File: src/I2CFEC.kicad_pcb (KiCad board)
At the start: 2 copper layers, 24 x 27.9 mm, 25 parts, among them J1 105444-0001, J2 B4B-XH-A, U1 PIC16F1454, U2 MIC2091

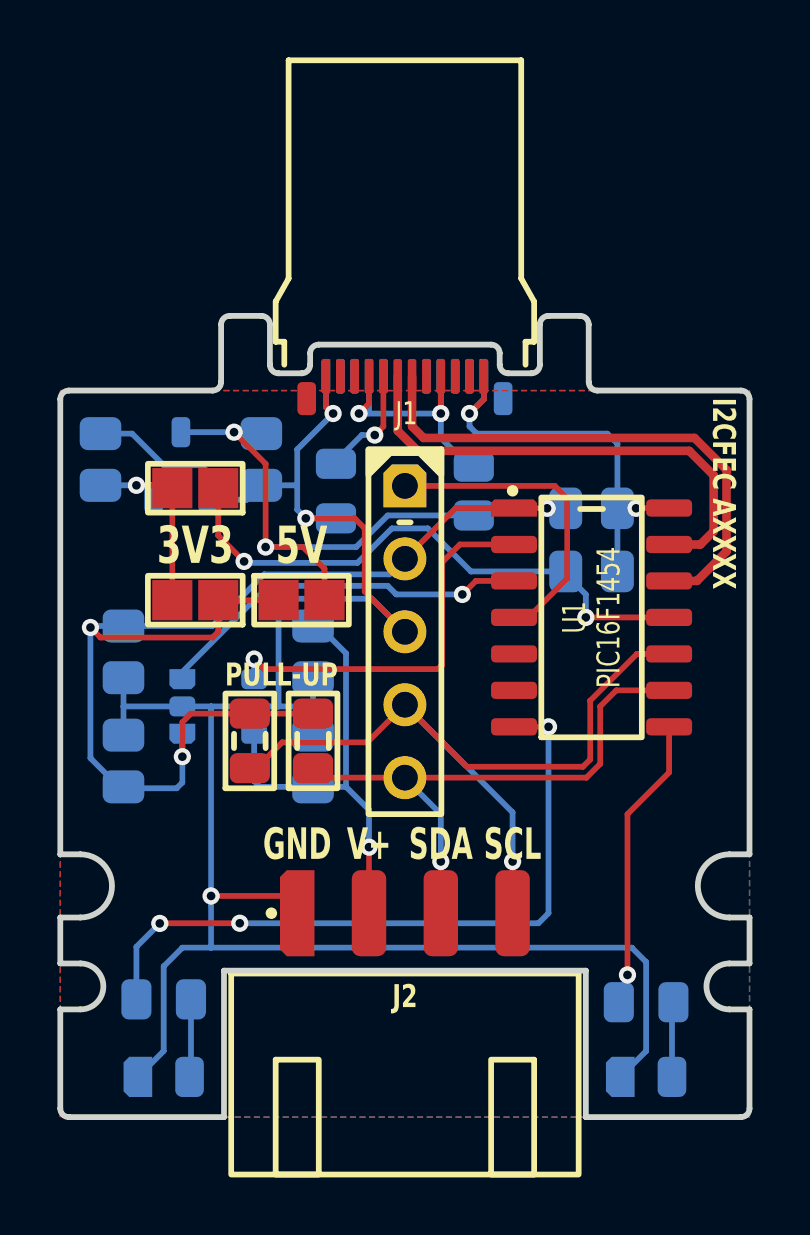
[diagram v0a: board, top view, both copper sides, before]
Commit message: Added pullup mosfet
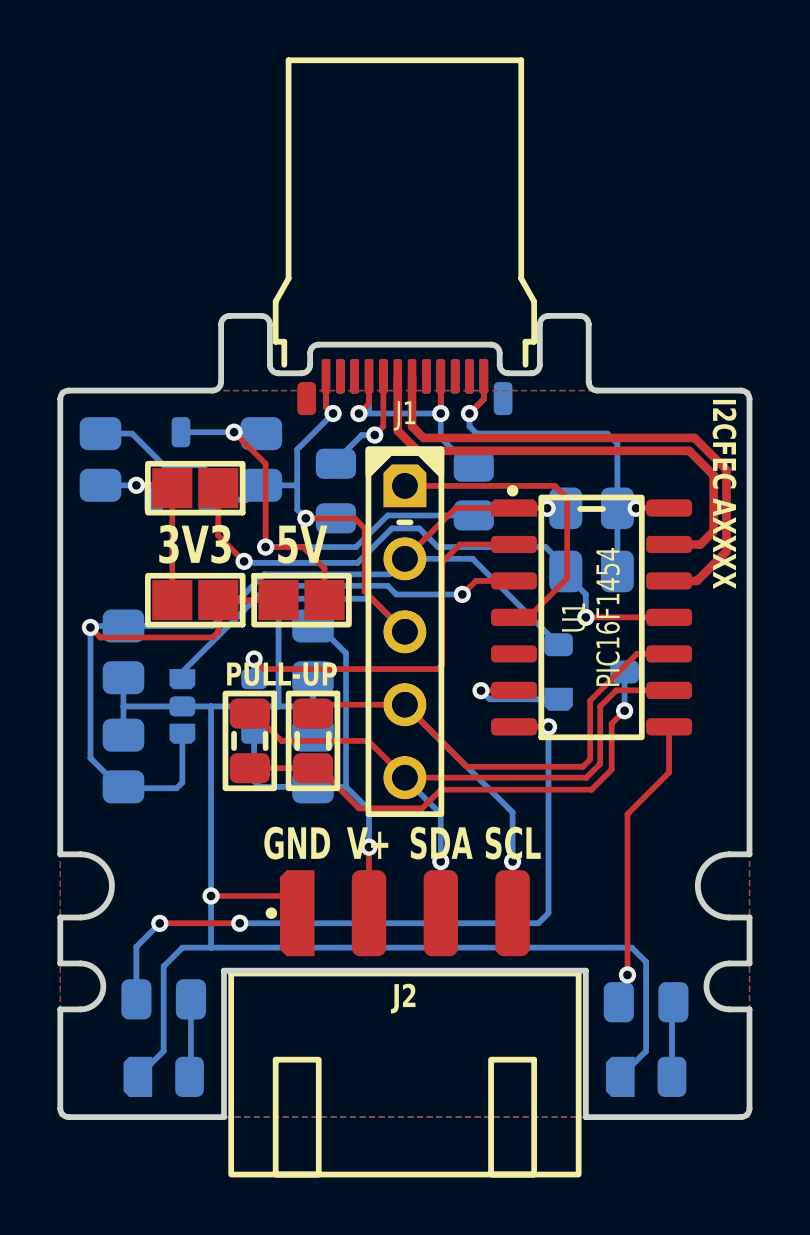
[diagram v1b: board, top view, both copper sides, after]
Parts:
- added Q1: BSS84, Medo64:Q MOSFET-P (SOT23-3), B.Cu at (38.5, 32.4)
- moved R3 2.20 mm to (28.8, 34.8), turned to -90 degrees
- moved R4 2.20 mm to (26.6, 34.8), turned to -90 degrees
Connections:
- R3 pad 2: VDD -> VDD_PULLUP
- R4 pad 2: VDD -> VDD_PULLUP
- U1 pad 6: (no net) -> OUT_PULLUP
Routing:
- net VDD_PULLUP: track 0.00 -> 17.1 mm, vias 0 -> 1
- net OUT_PULLUP: track 0.00 -> 3.98 mm, vias 0 -> 1
- net SDA: track 19.7 -> 23.0 mm
- net SCL: track 27.8 -> 24.6 mm
- net VDD: track 41.6 -> 42.3 mm, vias 3 -> 2
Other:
- board text added: "IOC ~{MCLR} Vpp"
- board text added: "RC5 T0CKI"
- board text added: "RX DT PWM1"

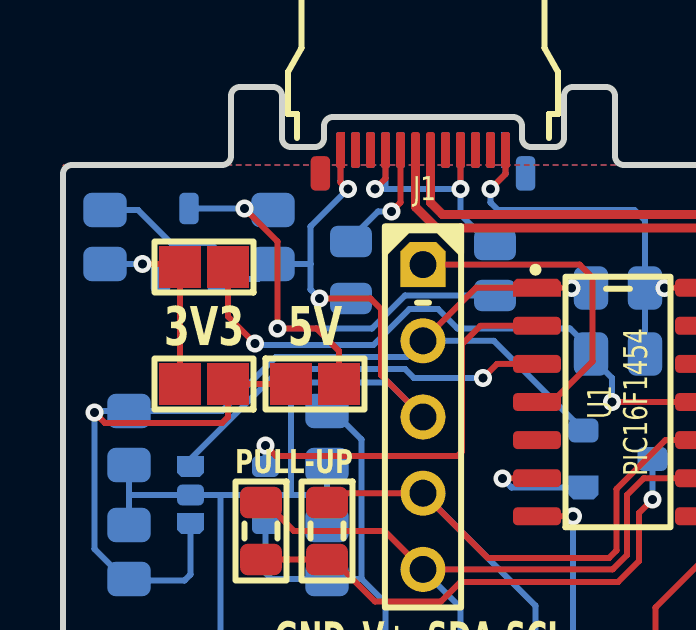
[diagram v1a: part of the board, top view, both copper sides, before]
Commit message: Adjusted 3.3/5V selection
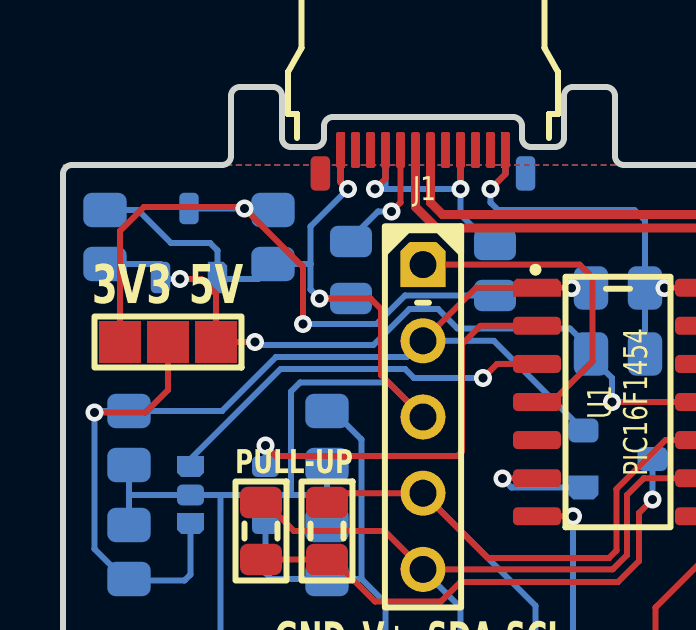
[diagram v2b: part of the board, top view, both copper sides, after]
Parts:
- removed JP2 (x3): Jumper, Medo64:JP (0805)
- added JP1: Jumper, Medo64:JP Dual (1205), F.Cu at (23.5, 28.5)
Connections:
- C4 pad 1: 3V3_USB -> 3V3
- U1 pad 11: 3V3_USB -> 3V3
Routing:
- net 3V3_USB: track 19.7 -> 0.00 mm, vias 2 -> 0
- net 3V3: track 7.95 -> 24.2 mm, vias 1 -> 3
- net 5V: track 19.3 -> 23.4 mm
- net VDD: track 42.3 -> 38.8 mm

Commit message: Moving components around - a lot
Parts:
- moved C6 18.8 mm to (38.8, 32.0), turned to 0 degrees
- moved C1 16.7 mm to (23.9, 34.8), turned to 90 degrees
- moved JP1 16.3 mm to (39.8, 29.0), turned to 90 degrees
- moved VR1 15.1 mm to (38.8, 29.0), turned to -90 degrees
- moved C5 11.8 mm to (38.8, 26.0), turned to 180 degrees
- moved R4 11.4 mm to (37.9, 36.5)
- moved R3 11.2 mm to (39.9, 36.5)
- moved ICSP 10.4 mm to (42.3, 29.4), turned to 90 degrees
- moved C2 9.33 mm to (28.9, 29.0)
- moved C4 7.20 mm to (31.3, 29.0), turned to -90 degrees
- moved U1 6.67 mm to (32.0, 29.0), turned to 90 degrees
- moved C8 5.14 mm to (32.9, 34.8), turned to 90 degrees
- moved R5 4.47 mm to (26.2, 29.0)
- moved Q1 4.08 mm to (39.0, 36.5)
- moved C7 3.14 mm to (21.7, 34.8), turned to 90 degrees
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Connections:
- U1 pad 2: POWER_FAULT -> POWER_EN
- U1 pad 3: POWER_EN -> POWER_FAULT
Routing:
- net 5V: track 23.4 -> 9.42 mm, vias 2 -> 1
- net USB_DM: track 18.6 -> 4.83 mm
- net USB_DP: track 17.2 -> 4.69 mm
- net LED_B: track 9.89 -> 22.3 mm
- net VDD_PULLUP: track 17.1 -> 4.73 mm
- net SCL: track 24.6 -> 36.0 mm, vias 1 -> 2
- net GND: track 94.6 -> 104.4 mm, vias 5 -> 7
- net POWER_EN: track 13.1 -> 5.35 mm
- net POWER_FAULT: track 13.8 -> 6.04 mm
- net 3V3: track 24.2 -> 17.3 mm, vias 3 -> 2
- net A_CC: track 3.83 -> 10.3 mm
- net VDD_OUT: track 15.7 -> 9.83 mm
- net OUT_PULLUP: track 3.98 -> 8.62 mm
- net SDA: track 23.0 -> 27.4 mm, vias 1 -> 2
- net VDD: track 38.8 -> 43.1 mm, vias 2 -> 4
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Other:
- board text removed: "IOC ~{MCLR} Vpp"
- board text removed: "RC5 T0CKI"
- board text removed: "RX DT PWM1"

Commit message: Refactoring some more
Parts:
- DS1: value IN -> UART
- DS2: value OUT -> I2C
- U1: value PIC16F1454 -> 16F1454
- moved C6 16.8 mm to (23.0, 26.2)
- moved VR1 15.8 mm to (23.0, 29.5), turned to 0 degrees
- moved JP1 15.8 mm to (24.0, 29.0), turned to 0 degrees
- moved C5 13.0 mm to (26.2, 29.0), turned to -90 degrees
- moved R4 9.50 mm to (37.8, 27.0)
- moved R3 9.50 mm to (39.9, 27.0), turned to 90 degrees
- moved Q1 7.45 mm to (39.0, 29.0)
- moved R5 5.91 mm to (23.1, 24.0), turned to 0 degrees
- turned L1 to 180 degrees
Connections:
- JP1 pad 1: 3V3 -> 5V
- JP1 pad 3: 5V -> 3V3
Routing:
- net SCL: track 36.0 -> 26.0 mm
- net 5V: track 9.42 -> 18.6 mm, vias 1 -> 2
- net GND: track 104.4 -> 108.2 mm, vias 7 -> 9
- net OUT_PULLUP: track 8.62 -> 5.71 mm
- net LED_B: track 22.3 -> 19.5 mm
- net 3V3: track 17.3 -> 15.9 mm
- net Vin: track 13.5 -> 14.5 mm
- net A_CC: track 10.3 -> 9.26 mm
- net SDA: track 27.4 -> 26.4 mm
- net LED_A: track 28.5 -> 27.6 mm
- net ICSP_VPP: track 12.8 -> 12.1 mm
- net VDD: track 43.1 -> 43.6 mm, vias 4 -> 3
